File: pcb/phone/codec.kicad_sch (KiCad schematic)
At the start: 10 parts, among them U3 ALC5651-CG, U9 TXB0108PWR

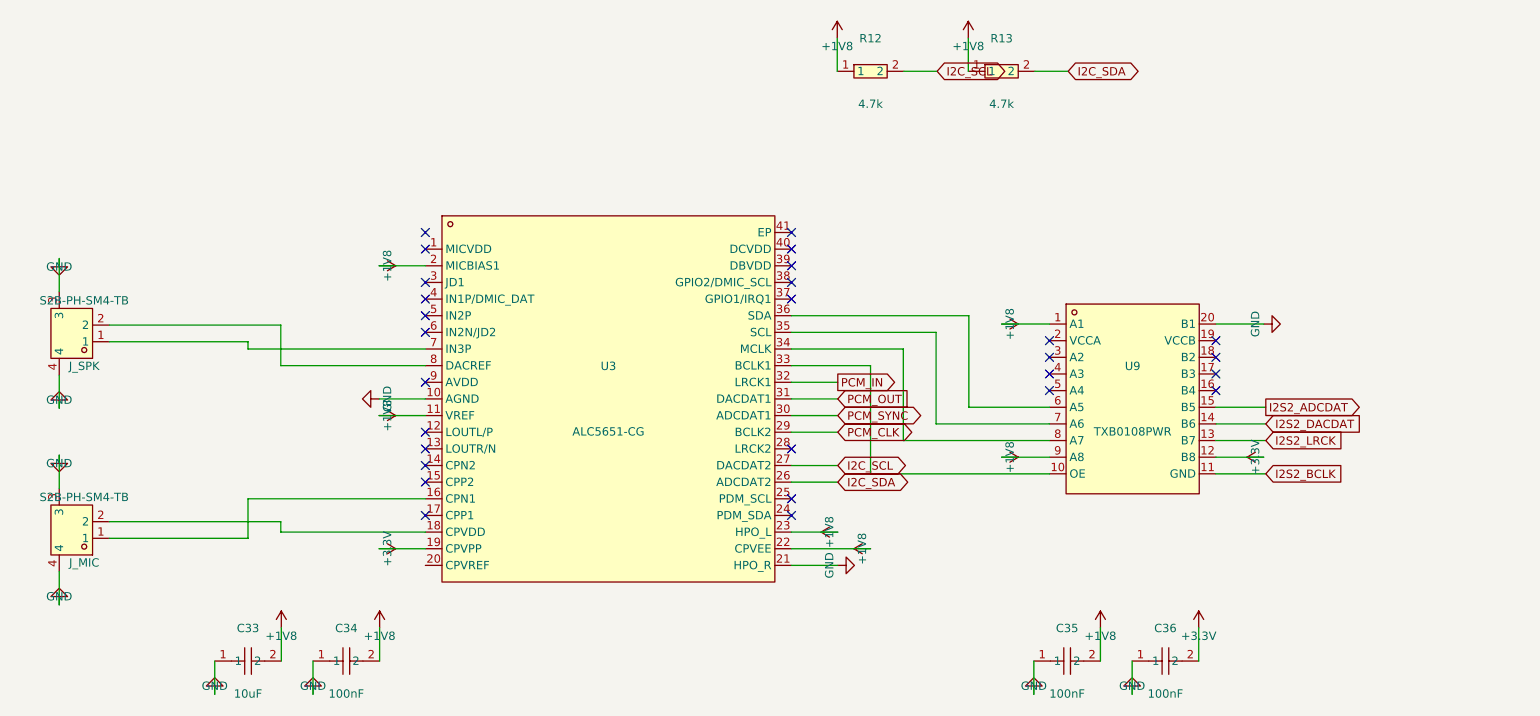
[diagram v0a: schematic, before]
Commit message: Fix codec sheet: flip ALC5651-CG and TXB0108PWR embedded symbols Y-axis
The codec subagent placed wires/NC flags at lib_symbol Y positions without
accounting for KiCad's Y-axis negation when rendering symbols. This caused
wires to connect to the wrong pins:

- Wire at Y=152.86 (+3.3V) connected to Pin 19 (CPVPP) instead of Pin 1 (MICVDD)
- Wire at Y=109.68 (+1V8) connected to Pin 2 (MICBIAS1) instead of Pin 18 (CPVDD)
- NC flags were on the wrong pins
- U9 (TXB0108PWR) had the same Y-mirroring issue

Fix: flip Y coordinates in the embedded ALC5651-CG and TXB0108PWR symbol
definitions in codec.kicad_sch only. This moves the pins to where the wires
and NC flags already are, fixing all connections.

Result: Codec sheet is now ERC-clean (0 errors, 0 warnings).
Total ERC violations dropped from 283 to 274.

Generated with [Devin](https://devin.ai)

Co-Authored-By: Devin <158243242+devin-ai-integration[bot]@users.noreply.github.com>
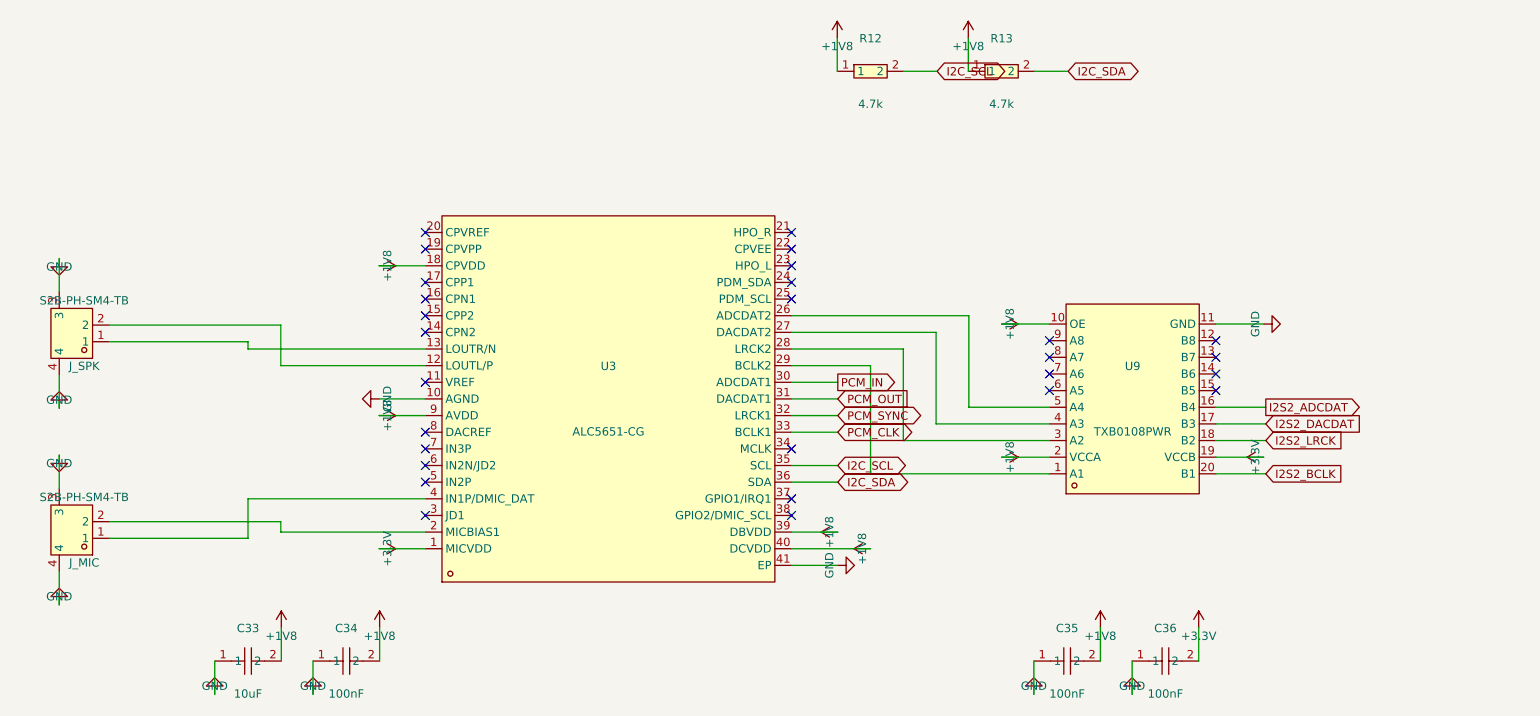
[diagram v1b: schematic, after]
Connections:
- net +1V8: now also U3.18 (CPVDD), U3.39 (DBVDD), U3.40 (DCVDD), U3.9 (AVDD), U9.10 (OE), U9.2 (VCCA); no longer U3.11 (VREF), U3.2 (MICBIAS1), U3.22 (CPVEE), U3.23 (HPO_L), U9.1 (A1), U9.9 (A8)
- net +3.3V: now also U3.1 (MICVDD), U9.19 (VCCB); no longer U3.19 (CPVPP), U9.12 (B8)
- net GND: now also U3.41 (EP), U9.11 (GND); no longer U3.21 (HPO_R), U9.20 (B1)
- net I2C_SCL: now also U3.35 (SCL); no longer U3.27 (DACDAT2)
- net I2C_SDA: now also U3.36 (SDA); no longer U3.26 (ADCDAT2)
- net I2S2_ADCDAT: now also U9.16 (B4); no longer U9.15 (B5)
- net I2S2_BCLK: now also U9.20 (B1); no longer U9.11 (GND)
- net I2S2_DACDAT: now also U9.17 (B3); no longer U9.14 (B6)
- net I2S2_LRCK: now also U9.18 (B2); no longer U9.13 (B7)
- net PCM_CLK: now also U3.33 (BCLK1); no longer U3.29 (BCLK2)
- net PCM_IN: now also U3.30 (ADCDAT1); no longer U3.32 (LRCK1)
- net PCM_SYNC: now also U3.32 (LRCK1); no longer U3.30 (ADCDAT1)
- net at U9.3 (A2): now also U3.28 (LRCK2)
- net at U9.4 (A3): now also U3.27 (DACDAT2)
- net at U9.5 (A4): now also U3.26 (ADCDAT2)
- net at U9.6 (A5): no longer U3.36 (SDA)
- net at U9.7 (A6): no longer U3.35 (SCL)
- net at U9.8 (A7): no longer U3.34 (MCLK)
- net at J_MIC.1: now also U3.4 (IN1P/DMIC_DAT); no longer U3.16 (CPN1)
- net at J_MIC.2: now also U3.2 (MICBIAS1); no longer U3.18 (CPVDD)
- net at J_SPK.1: now also U3.13 (LOUTR/N); no longer U3.7 (IN3P)
- net at J_SPK.2: now also U3.12 (LOUTL/P); no longer U3.8 (DACREF)
- new net: U3.29 (BCLK2), U9.1 (A1)

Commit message: User edits: keypad rewiring, sheet reorder, ERC severity reverts, R24 fix
Keypad (keypad.kicad_sch):
- Rotated all 20 switches 270 degrees for vertical contact orientation
- Wired all 4 pins on each switch (pins 1&2 to column, pins 3&4 to row)
- Removed all 37 no_connect markers on pins 3&4
- Cleaned up to 25.4mm (1-inch) grid spacing
- Added pull-down resistors to all 4 columns (was only KEY_COL3)

Root sheet (phone.kicad_sch):
- Reordered sub-sheet blocks (Display_Daughter before SIM_SD)
- Cleaned up PWR_FLAG symbol formatting/indentation
- Reordered PWR_FLAG and +BATT symbol placement

MCU sheet (mcu.kicad_sch):
- Repositioned +3.3V power symbol (#PWR32) at pin 190.5,200.66

Project settings (phone.kicad_pro):
- Reverted ERC suppressions: endpoint_off_grid, isolated_pin_label,
  lib_symbol_mismatch back to warning (want actual fixes, not ignores)
- Added SW2-20 to used designators
- Reordered sheets list (Display_Daughter before SIM_SD)

Other sheets (codec, display, display_daughter, sim_sd):
- KiCad editor reformatting upon save

Generated with [Devin](https://devin.ai)

Co-Authored-By: Devin <158243242+devin-ai-integration[bot]@users.noreply.github.com>
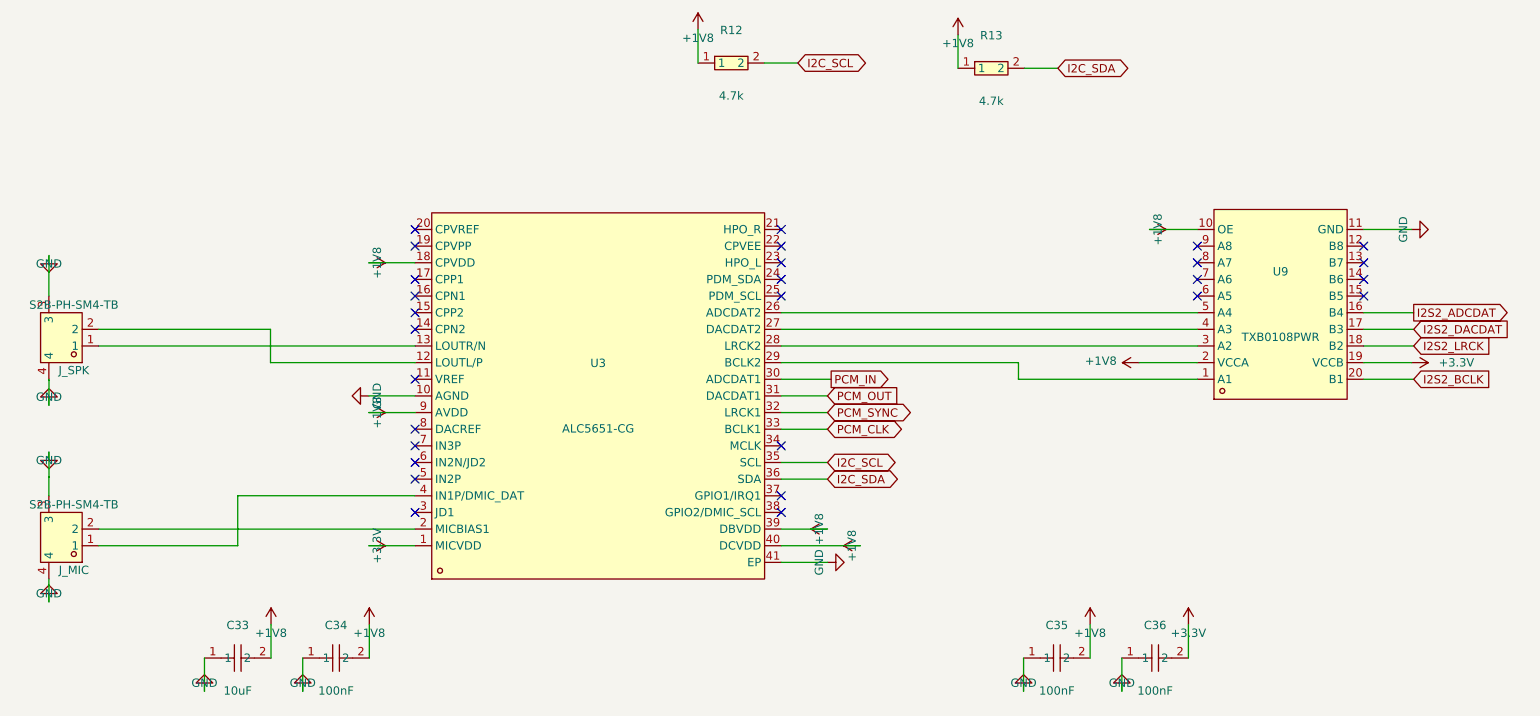
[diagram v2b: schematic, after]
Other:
- moved on the sheet: C33, C34, C35, C36, J_MIC, J_SPK, R12, R13, U3, U9
